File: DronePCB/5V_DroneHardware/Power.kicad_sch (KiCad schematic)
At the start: 8 parts

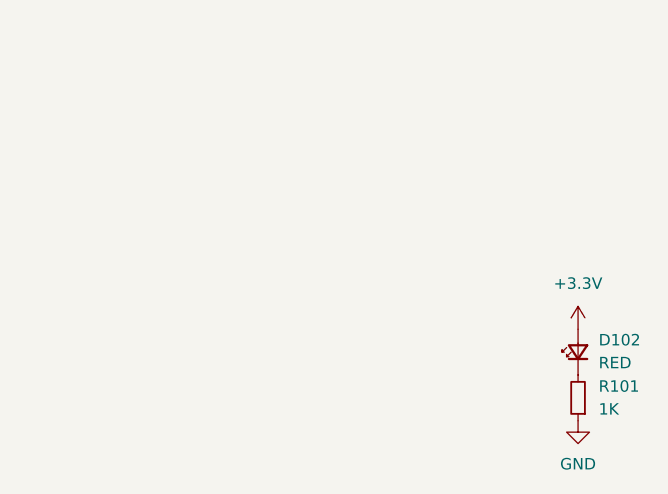
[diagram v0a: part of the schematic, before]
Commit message: Creazione della scheda con il convertitore da 5V a 3.3V
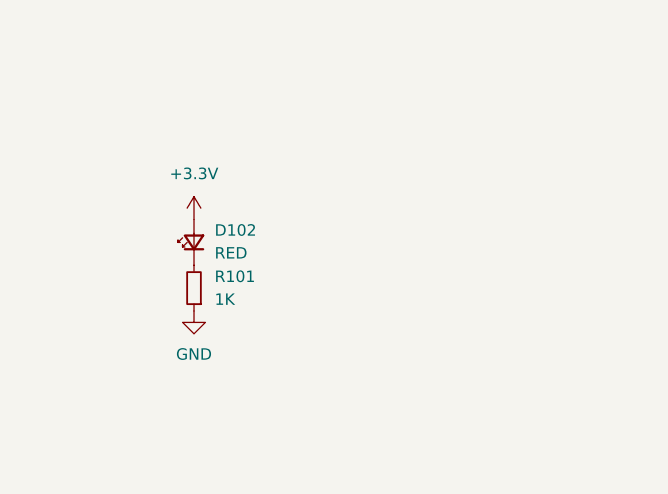
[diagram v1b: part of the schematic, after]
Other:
- moved on the sheet: D102, R101
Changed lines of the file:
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@@
     (pin "2")
   )
-  (symbol (lib_id "Device:LED_Small") (at 272.288 99.822 90) (unit 1)
+  (symbol (lib_id "Device:LED_Small") (at 229.616 87.63 90) (unit 1)
     (in_bom yes) (on_board yes) (fields_autoplaced)
-    (property "Reference" "D102" (id 0) (at 274.574 98.4884 90)
+    (property "Reference" "D102" (id 0) (at 231.902 86.2964 90)
       (effects (font (size 1.27 1.27)) (justify right))
     )
-    (property "Value" "RED" (id 1) (at 274.574 101.0284 90)
+    (property "Value" "RED" (id 1) (at 231.902 88.8364 90)
       (effects (font (size 1.27 1.27)) (justify right))
     )
-    (property "Footprint" "LED_SMD:LED_0603_1608Metric" (id 2) (at 272.288 99.822 90)
+    (property "Footprint" "LED_SMD:LED_0603_1608Metric" (id 2) (at 229.616 87.63 90)
       (effects (font (size 1.27 1.27)) hide)
     )
-    (property "Datasheet" "https://jlcpcb.com/parts/componentSearch?isSearch=true&searchTxt=12pf%200402" (id 3) (at 272.288 99.822 90)
+    (property "Datasheet" "https://jlcpcb.com/parts/componentSearch?isSearch=true&searchTxt=12pf%200402" (id 3) (at 229.616 87.63 90)
       (effects (font (size 1.27 1.27)) hide)
     )
-    (property "LCSC Part #" "C2286" (id 4) (at 272.288 99.822 0)
+    (property "LCSC Part #" "C2286" (id 4) (at 229.616 87.63 0)
       (effects (font (size 1.27 1.27)) hide)
     )
@@
     (pin "2")
   )
-  (symbol (lib_id "power:GND") (at 272.288 107.442 0) (unit 1)
+  (symbol (lib_id "power:GND") (at 229.616 95.25 0) (unit 1)
     (in_bom yes) (on_board yes) (fields_autoplaced)
-    (property "Reference" "#PWR0105" (id 0) (at 272.288 113.792 0)
+    (property "Reference" "#PWR0105" (id 0) (at 229.616 101.6 0)
       (effects (font (size 1.27 1.27)) hide)
     )
-    (property "Value" "GND" (id 1) (at 272.288 112.268 0))
-    (property "Footprint" "" (id 2) (at 272.288 107.442 0)
+    (property "Value" "GND" (id 1) (at 229.616 100.076 0))
+    (property "Footprint" "" (id 2) (at 229.616 95.25 0)
       (effects (font (size 1.27 1.27)) hide)
     )
-    (property "Datasheet" "" (id 3) (at 272.288 107.442 0)
+    (property "Datasheet" "" (id 3) (at 229.616 95.25 0)
       (effects (font (size 1.27 1.27)) hide)
     )
@@
     (pin "2")
   )
-  (symbol (lib_id "power:+3.3V") (at 272.288 97.282 0) (unit 1)
+  (symbol (lib_id "power:+3.3V") (at 229.616 85.09 0) (unit 1)
     (in_bom yes) (on_board yes) (fields_autoplaced)
-    (property "Reference" "#PWR0104" (id 0) (at 272.288 101.092 0)
+    (property "Reference" "#PWR0104" (id 0) (at 229.616 88.9 0)
       (effects (font (size 1.27 1.27)) hide)
     )
-    (property "Value" "+3.3V" (id 1) (at 272.288 92.202 0))
-    (property "Footprint" "" (id 2) (at 272.288 97.282 0)
+    (property "Value" "+3.3V" (id 1) (at 229.616 80.01 0))
+    (property "Footprint" "" (id 2) (at 229.616 85.09 0)
       (effects (font (size 1.27 1.27)) hide)
     )
-    (property "Datasheet" "" (id 3) (at 272.288 97.282 0)
+    (property "Datasheet" "" (id 3) (at 229.616 85.09 0)
       (effects (font (size 1.27 1.27)) hide)
     )
@@
     (pin "2")
   )
-  (symbol (lib_id "Device:R_Small") (at 272.288 104.902 180) (unit 1)
+  (symbol (lib_id "Device:R_Small") (at 229.616 92.71 180) (unit 1)
     (in_bom yes) (on_board yes) (fields_autoplaced)
-    (property "Reference" "R101" (id 0) (at 274.574 103.6319 0)
+    (property "Reference" "R101" (id 0) (at 231.902 91.4399 0)
       (effects (font (size 1.27 1.27)) (justify right))
     )
-    (property "Value" "1K" (id 1) (at 274.574 106.1719 0)
+    (property "Value" "1K" (id 1) (at 231.902 93.9799 0)
       (effects (font (size 1.27 1.27)) (justify right))
     )
-    (property "Footprint" "Resistor_SMD:R_0603_1608Metric" (id 2) (at 272.288 104.902 0)
+    (property "Footprint" "Resistor_SMD:R_0603_1608Metric" (id 2) (at 229.616 92.71 0)
       (effects (font (size 1.27 1.27)) hide)
     )
-    (property "Datasheet" "~" (id 3) (at 272.288 104.902 0)
+    (property "Datasheet" "~" (id 3) (at 229.616 92.71 0)
       (effects (font (size 1.27 1.27)) hide)
     )
-    (property "LCSC Part #" "C21190" (id 4) (at 272.288 104.902 0)
+    (property "LCSC Part #" "C21190" (id 4) (at 229.616 92.71 0)
       (effects (font (size 1.27 1.27)) hide)
     )

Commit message: Aggiunta dell'alimentazine della radio e il GND
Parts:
- added J101: +5V, Connector_PinHeader_1.00mm:PinHeader_1x01_P1.00mm_Vertical, symbol Connector:Conn_01x01_Male
- added J102: GND, Connector_PinHeader_1.00mm:PinHeader_1x04_P1.00mm_Vertical, symbol Connector:Conn_01x04_Male
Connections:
- net BUCK_IN: now also J101.1 (Pin_1)
- net GND: now also J102.1 (Pin_1), J102.2 (Pin_2), J102.3 (Pin_3), J102.4 (Pin_4)
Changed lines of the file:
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@@
   (junction (at 161.036 91.44) (diameter 0) (color 0 0 0 0)
   )
+  (junction (at 117.602 146.812) (diameter 0) (color 0 0 0 0)
+  )
   (junction (at 68.326 81.026) (diameter 0) (color 0 0 0 0)
   )
@@
   (junction (at 167.132 81.788) (diameter 0) (color 0 0 0 0)
   )
+  (junction (at 117.602 141.732) (diameter 0) (color 0 0 0 0)
+  )
+  (junction (at 117.602 144.272) (diameter 0) (color 0 0 0 0)
+  )
   (polyline (pts (xy 68.834 102.108) (xy 68.834 95.504))
     (stroke (width 0) (type default) (color 0 0 0 0))
@@
     (stroke (width 0) (type default) (color 0 0 0 0))
   )
+  (wire (pts (xy 123.444 139.192) (xy 117.602 139.192))
+    (stroke (width 0) (type default) (color 0 0 0 0))
+  )
   (wire (pts (xy 161.036 91.44) (xy 161.036 93.218))
     (stroke (width 0) (type default) (color 0 0 0 0))
@@
     (stroke (width 0) (type default) (color 0 0 0 0))
   )
+  (wire (pts (xy 117.602 144.272) (xy 123.444 144.272))
+    (stroke (width 0) (type default) (color 0 0 0 0))
+  )
   (polyline (pts (xy 49.276 85.852) (xy 58.674 85.852))
     (stroke (width 0) (type default) (color 0 0 0 0))
@@
     (stroke (width 0) (type default) (color 0 0 0 0))
   )
+  (wire (pts (xy 117.602 141.732) (xy 123.444 141.732))
+    (stroke (width 0) (type default) (color 0 0 0 0))
+  )
+  (wire (pts (xy 117.602 139.192) (xy 117.602 141.732))
+    (stroke (width 0) (type default) (color 0 0 0 0))
+  )
   (wire (pts (xy 161.036 86.868) (xy 161.036 89.408))
     (stroke (width 0) (type default) (color 0 0 0 0))
@@
     (stroke (width 0) (type default) (color 0 0 0 0))
   )
+  (wire (pts (xy 117.602 144.272) (xy 117.602 146.812))
+    (stroke (width 0) (type default) (color 0 0 0 0))
+  )
+  (wire (pts (xy 117.602 146.812) (xy 123.444 146.812))
+    (stroke (width 0) (type default) (color 0 0 0 0))
+  )
+  (wire (pts (xy 117.602 141.732) (xy 117.602 144.272))
+    (stroke (width 0) (type default) (color 0 0 0 0))
+  )
   (polyline (pts (xy 49.276 93.98) (xy 49.276 85.852))
     (stroke (width 0) (type default) (color 0 0 0 0))
@@
   )
   (wire (pts (xy 45.466 81.026) (xy 50.8 81.026))
+    (stroke (width 0) (type default) (color 0 0 0 0))
+  )
+  (wire (pts (xy 117.602 146.812) (xy 117.602 150.876))
     (stroke (width 0) (type default) (color 0 0 0 0))
   )
@@
     )
   )
+  (global_label "BUCK_IN" (shape input) (at 123.444 126.238 180) (fields_autoplaced)
+    (effects (font (size 1.27 1.27)) (justify right))
+    (property "Intersheet References" "${INTERSHEET_REFS}" (id 0) (at 112.9876 126.1586 0)
+      (effects (font (size 1.27 1.27)) (justify right) hide)
+    )
+  )
+  (symbol (lib_id "power:GND") (at 117.602 150.876 0) (unit 1)
+    (in_bom yes) (on_board yes) (fields_autoplaced)
+    (property "Reference" "#PWR0106" (id 0) (at 117.602 157.226 0)
+      (effects (font (size 1.27 1.27)) hide)
+    )
+    (property "Value" "GND" (id 1) (at 117.602 155.702 0))
+    (property "Footprint" "" (id 2) (at 117.602 150.876 0)
+      (effects (font (size 1.27 1.27)) hide)
+    )
+    (property "Datasheet" "" (id 3) (at 117.602 150.876 0)
+      (effects (font (size 1.27 1.27)) hide)
+    )
+    (pin "1")
+  )
   (symbol (lib_id "Device:D_Schottky_Small") (at 45.466 78.486 90) (unit 1)
     (in_bom yes) (on_board yes)
@@
     (pin "1")
   )
+  (symbol (lib_id "Connector:Conn_01x01_Male") (at 128.524 126.238 180) (unit 1)
+    (in_bom yes) (on_board yes) (fields_autoplaced)
+    (property "Reference" "J101" (id 0) (at 127.889 120.65 0))
+    (property "Value" "+5V" (id 1) (at 127.889 123.19 0))
+    (property "Footprint" "Connector_PinHeader_1.00mm:PinHeader_1x01_P1.00mm_Vertical" (id 2) (at 128.524 126.238 0)
+      (effects (font (size 1.27 1.27)) hide)
+    )
+    (property "Datasheet" "~" (id 3) (at 128.524 126.238 0)
+      (effects (font (size 1.27 1.27)) hide)
+    )
+    (pin "1")
+  )
+  (symbol (lib_id "Connector:Conn_01x04_Male") (at 128.524 144.272 180) (unit 1)
+    (in_bom yes) (on_board yes) (fields_autoplaced)
+    (property "Reference" "J102" (id 0) (at 129.54 141.7319 0)
+      (effects (font (size 1.27 1.27)) (justify right))
+    )
+    (property "Value" "GND" (id 1) (at 129.54 144.2719 0)
+      (effects (font (size 1.27 1.27)) (justify right))
+    )
+    (property "Footprint" "Connector_PinHeader_1.00mm:PinHeader_1x04_P1.00mm_Vertical" (id 2) (at 128.524 144.272 0)
+      (effects (font (size 1.27 1.27)) hide)
+    )
+    (property "Datasheet" "~" (id 3) (at 128.524 144.272 0)
+      (effects (font (size 1.27 1.27)) hide)
+    )
+    (pin "1")
+    (pin "2")
+    (pin "3")
+    (pin "4")
+  )
   (symbol (lib_id "Device:Polyfuse_Small") (at 53.34 81.026 90) (unit 1)

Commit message: BOM e pos file
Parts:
- C102: footprint Capacitor_SMD:C_0201_0603Metric -> Capacitor_Tantalum_SMD:CP_EIA-1608-08_AVX-J; LCSC Part # (none) -> C347532
- VR101: LCSC Part # (none) -> C140319
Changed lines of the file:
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@@
       (effects (font (size 1.27 1.27)) (justify left))
     )
-    (property "Footprint" "Capacitor_SMD:C_0201_0603Metric" (id 2) (at 168.0972 91.186 0)
+    (property "Footprint" "Capacitor_Tantalum_SMD:CP_EIA-1608-08_AVX-J" (id 2) (at 168.0972 91.186 0)
       (effects (font (size 1.27 1.27)) hide)
     )
     (property "Datasheet" "~" (id 3) (at 167.132 87.376 0)
+      (effects (font (size 1.27 1.27)) hide)
+    )
+    (property "LCSC Part #" "C347532" (id 4) (at 167.132 87.376 0)
       (effects (font (size 1.27 1.27)) hide)
     )
@@
       (effects (font (size 1.27 1.27)) (justify left bottom) hide)
     )
+    (property "LCSC Part #" "C140319" (id 8) (at 141.478 84.328 0)
+      (effects (font (size 1.27 1.27)) hide)
+    )
     (pin "1")
